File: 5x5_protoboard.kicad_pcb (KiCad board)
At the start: 2 copper layers, 50 x 50 mm, 90 parts, among them CON1 BARREL_JACK, CON2 USB-MINI-B, CON3 USB-MICRO, J1 PINS_3X1, J10 PINS_3X1, J11 PINS_3X1, J12 PINS_3X1, J13 PINS_3X1, J14 PINS_3X1, J15 PINS_3X1, J16 PINS_3X1, J17 PINS_3X1, J18 PINS_3X1, J19 PINS_3X1, J2 PINS_3X1, J20 PINS_3X1, J21 PINS_3X1, J22 PINS_3X1, J23 PINS_3X1, J24 PINS_3X1, J25 PINS_3X1, J26 PINS_3X1, J27 PINS_3X1, J28 PINS_3X1, J29 PINS_3X1, J3 PINS_3X1, J30 PINS_3X1, J31 PINS_3X1, J32 PINS_3X1, J33 PINS_3X1, J34 PINS_3X1, J35 PINS_3X1, J36 PINS_3X1, J37 PINS_3X1, J38 PINS_3X1, J39 PINS_3X1, J4 PINS_3X1, J40 PINS_3X1, J41 PINS_3X1, J42 PINS_3X1, J43 PINS_3X1, J44 PINS_3X1, J45 PINS_3X1, J46 PINS_3X1, J47 PINS_3X1, J48 PINS_3X1, J49 PINS_3X1, J5 PINS_3X1, J50 PINS_3X1, J51 PINS_3X1, J52 PINS_3X1, J53 PINS_3X1, J54 PINS_3X1, J55 PINS_3X1, J56 PINS_3X1, J57 PINS_3X1, J58 PINS_3X1, J59 PINS_3X1, J6 PINS_3X1, J60 PINS_3X1, J61 PINS_3X1, J62 PINS_3X1, J63 PINS_3X1, J64 PINS_3X1, J65 PINS_2X1, J7 PINS_3X1, J8 PINS_3X1, J9 PINS_3X1, P1 CONN_5, U1 7805

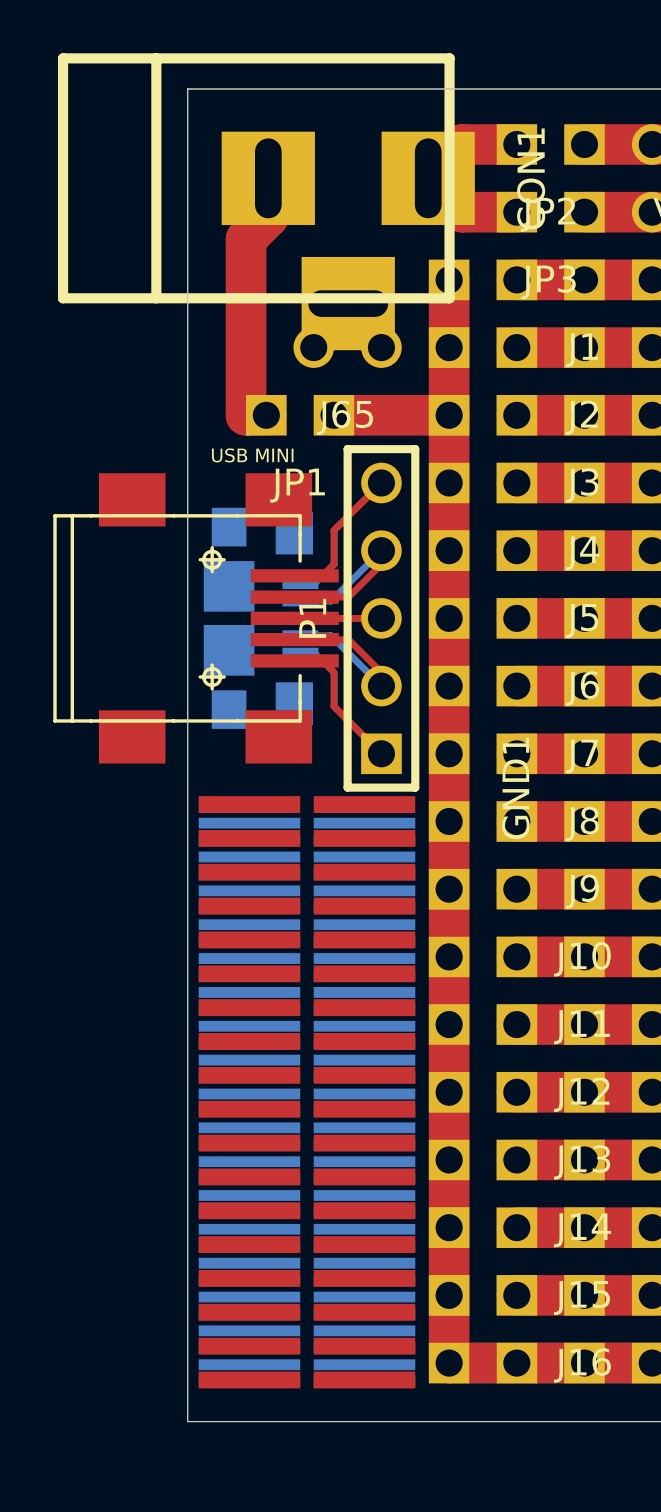
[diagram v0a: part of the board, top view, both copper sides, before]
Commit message: added pads for PTC 1812(SMD) fuse on both sides of the PCB between GND and the barrel jack on the same spot as the jumper and in parallel with it and eachother
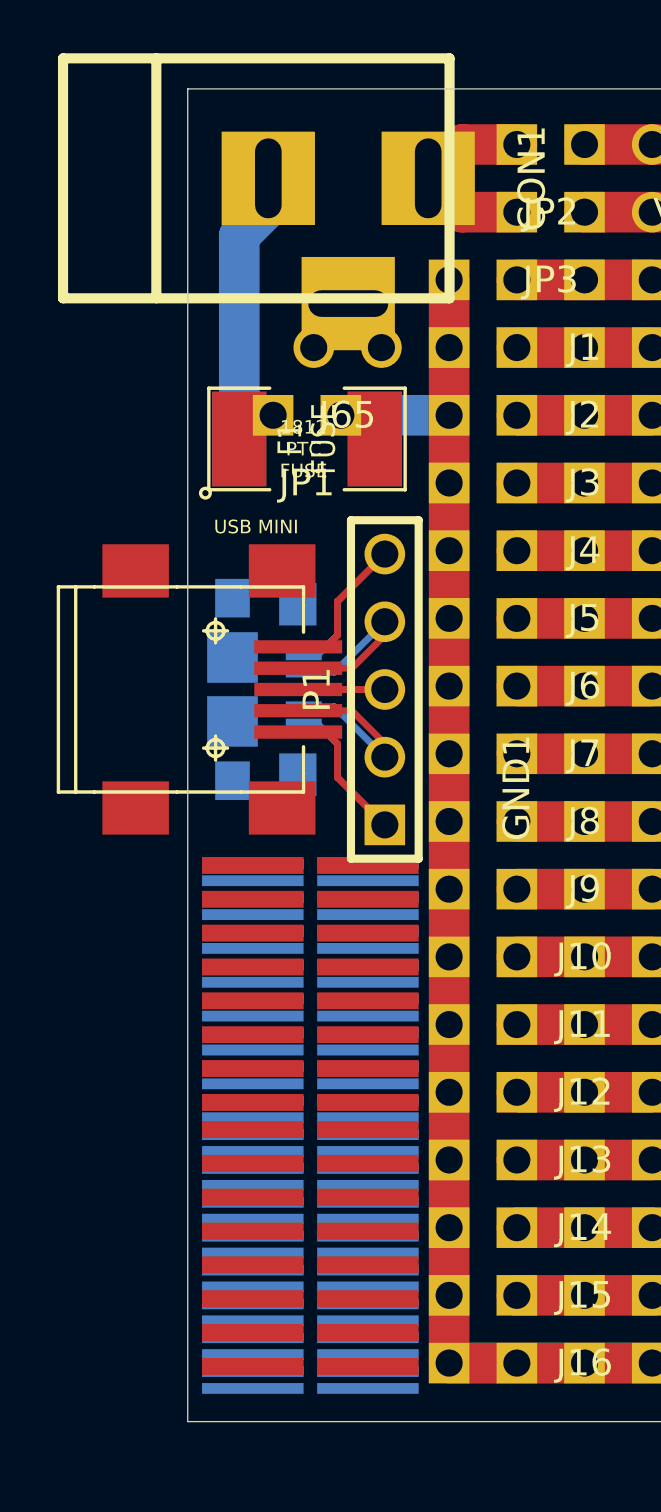
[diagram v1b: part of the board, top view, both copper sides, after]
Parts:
- removed the Ref** at (34.0, 49.5)
- removed the Ref** at (34.0, 49.9)
- added F1: FUSE, SM1812L, F.Cu at (34.0, 35.2)
- added F2: FUSE, SM1812L, B.Cu at (34.0, 35.2)
- moved CON3 2.67 mm to (31.2, 44.6)
- moved P1 2.67 mm to (37.0, 44.6)
- moved CON2 2.67 mm to (30.6, 44.6)
- moved Ref** 0.52 mm to (34.2, 65.5)
- moved Ref** 0.28 mm to (34.2, 55.6)
- moved Ref** 0.28 mm to (34.2, 68.6)
- moved Ref** 0.28 mm to (34.2, 58.4)
- moved Ref** 0.28 mm to (34.2, 53.3)
- moved Ref** 0.28 mm to (34.2, 63.5)
- moved JP1 0.25 mm to (34.0, 34.3)
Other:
- board text added: "1812 PTC"
- board text added: "1812 PTC FUSE"

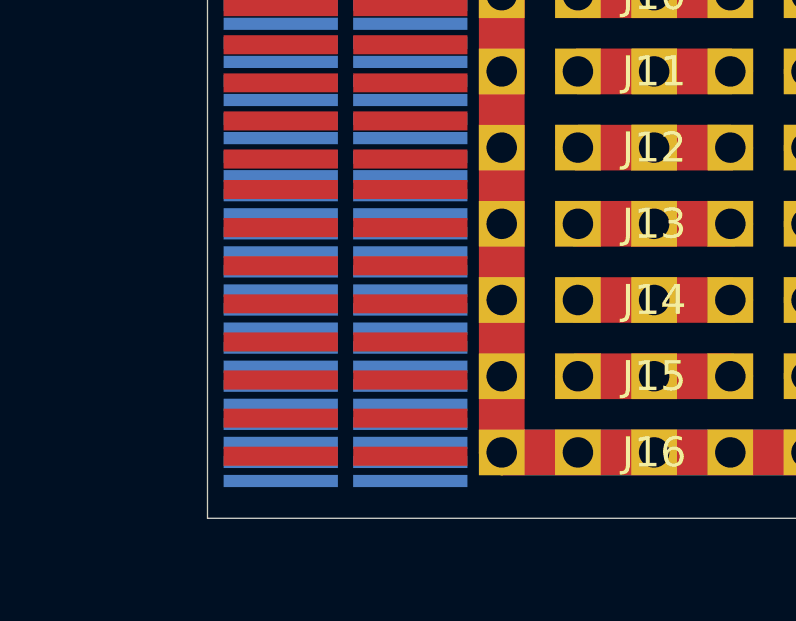
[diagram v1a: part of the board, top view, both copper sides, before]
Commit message: fixed SMD 1.27mm alignment and removed some accidental text on F.Mask
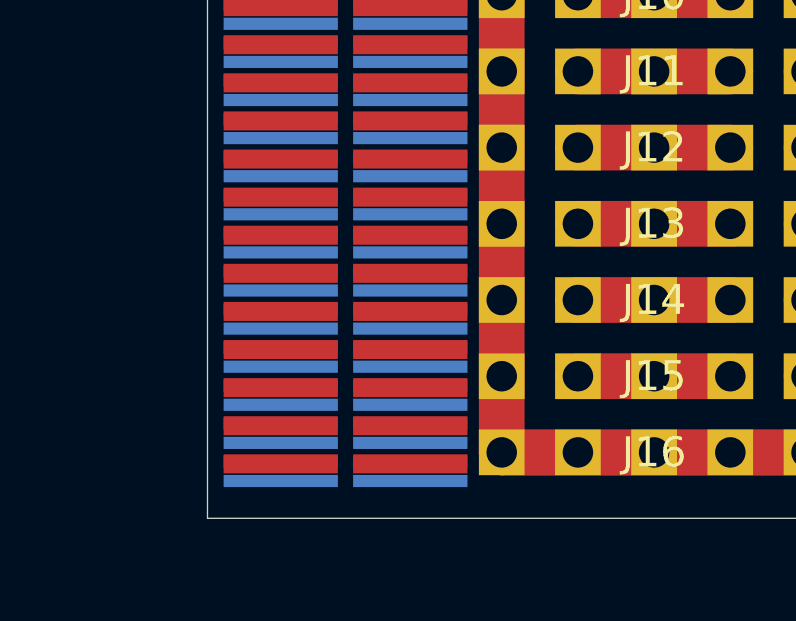
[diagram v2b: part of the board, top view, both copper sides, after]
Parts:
- moved Ref** 0.25 mm to (34.2, 65.8)
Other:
- board text removed: "1812 PTC"
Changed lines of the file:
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@@
     (links 236)
     (no_connects 158)
-    (area 29.549299 22.033299 79.574701 72.058701)
+    (area 24.391619 18.53692 80.839 73.219)
     (thickness 1.6)
-    (drawings 10)
+    (drawings 9)
     (tracks 115)
     (zones 0)
@@
     (pad_to_mask_clearance 0)
     (aux_axis_origin 0 0)
-    (visible_elements FFFFFF8F)
+    (visible_elements FFFFFE8F)
     (pcbplotparams
       (layerselection 284196865)
@@
       (drillshape 0)
       (scaleselection 1)
-      (outputdirectory 5x5_protoboard/))
+      (outputdirectory 5x5_protoboard_v1/))
   )
   (net 0 "")
@@
   )
   (module SMD_127_381_8X2 (layer F.Cu)
-    (at 34.163 65.532)
+    (at 34.163 65.786)
     (fp_text reference Ref** (at 0 0) (layer F.SilkS) hide
       (effects (font (size 1 1) (thickness 0.15)))
@@
     (effects (font (size 0.508 0.508) (thickness 0.127)))
   )
-  (gr_text "1812\nPTC" (at 33.782 36.449) (layer F.Mask)
-    (effects (font (size 0.2 0.2) (thickness 0.05)) (justify mirror))
-  )
   (gr_text "USB MICRO" (at 32.639 39.751) (layer B.SilkS)

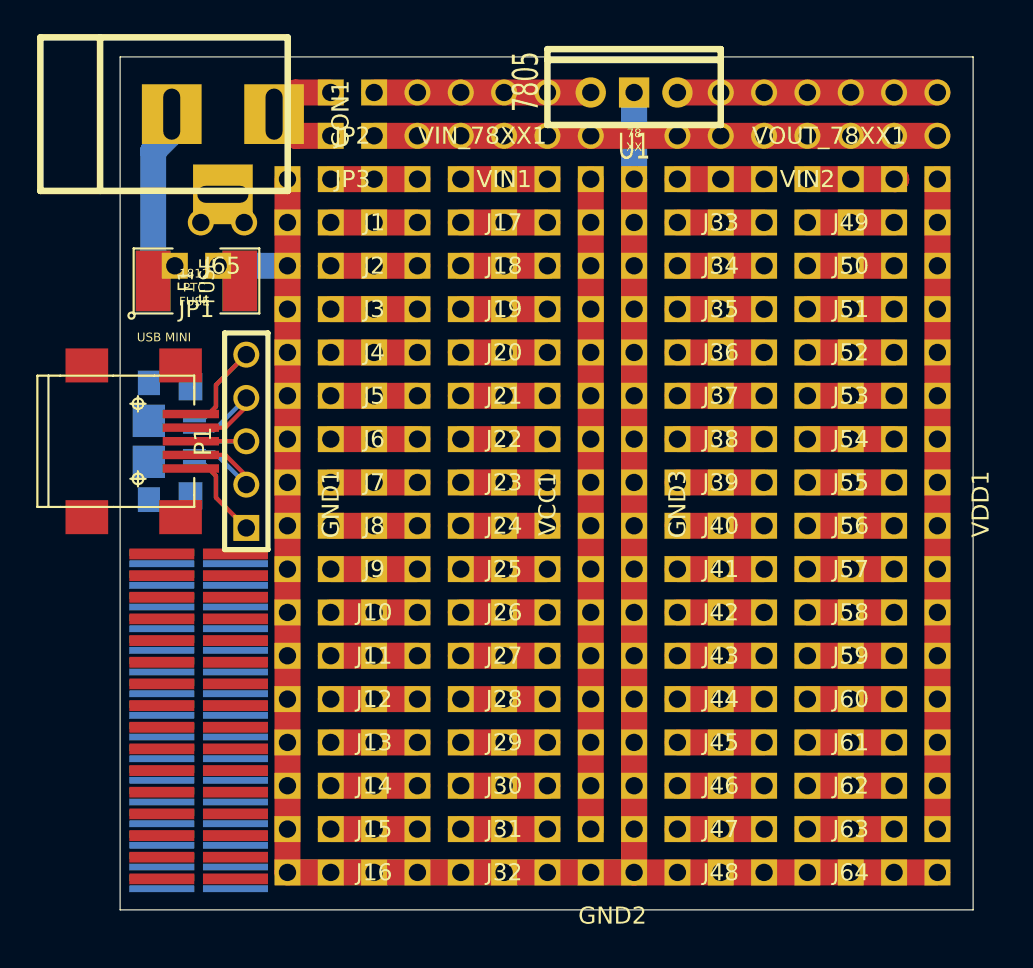
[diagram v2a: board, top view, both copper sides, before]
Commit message: fixed usb pin header alignment to the other pads and the added traces to both sides of the interconnects
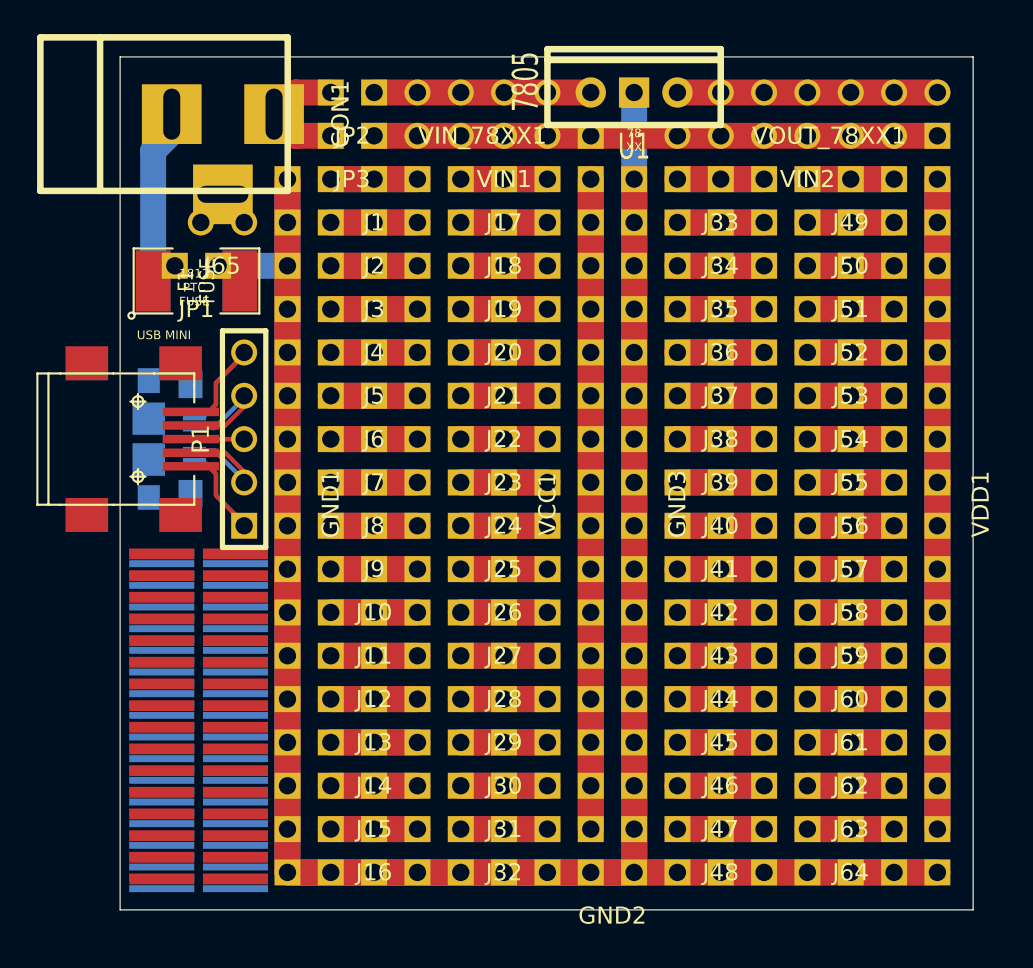
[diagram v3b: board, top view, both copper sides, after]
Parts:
- moved P1 0.18 mm to (36.8, 44.5)
- moved CON2 0.13 mm to (30.6, 44.5)
- moved CON3 0.13 mm to (31.2, 44.5)
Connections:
- U1 pad 1: (no net) -> N-0000056
- U1 pad 2: (no net) -> N-0000084
- U1 pad 3: (no net) -> N-0000059
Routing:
- net N-0000084: track 230.1 -> 352.0 mm
- net N-0000042: track 38.1 -> 76.2 mm
- net N-0000041: track 38.1 -> 76.2 mm
- net N-0000059: track 0.00 -> 15.2 mm
- net (no net): track 21.5 -> 6.29 mm
- net N-0000086: track 5.08 -> 10.2 mm
- net N-0000082: track 5.08 -> 10.2 mm
- net N-0000081: track 5.08 -> 10.2 mm
- net N-0000079: track 5.08 -> 10.2 mm
- net N-0000076: track 5.08 -> 10.2 mm
- net N-0000074: track 5.08 -> 10.2 mm
- net N-0000066: track 5.08 -> 10.2 mm
- net N-0000058: track 5.08 -> 10.2 mm
- net N-0000054: track 5.08 -> 10.2 mm
- net N-0000052: track 5.08 -> 10.2 mm
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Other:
- net class Interconnect removed
- net class Power added: clearance 0.254, trace_width 1.524, via_dia 0.889, via_drill 0.635

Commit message: recreated board using interconnect modules increased rails/triplet pad size, added solder jumper in addition to pin jumpers and added text for USB micro/mini pinout
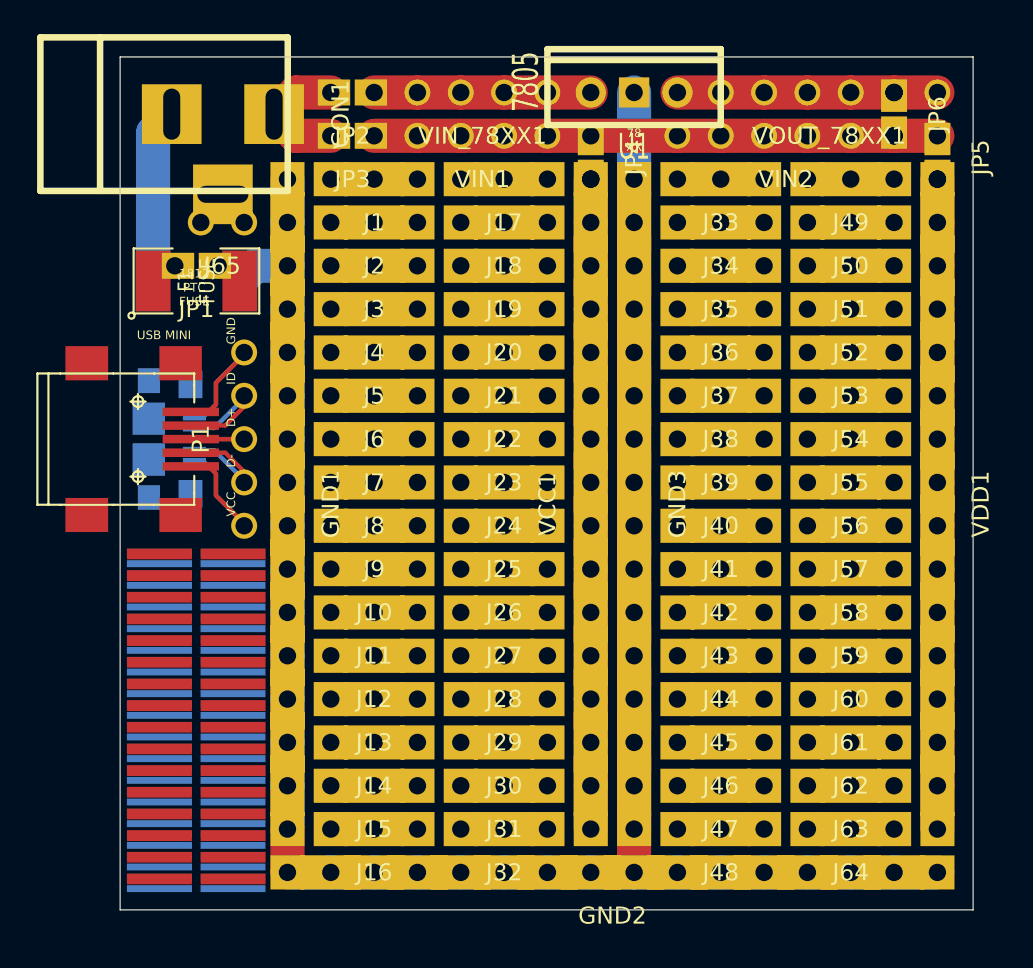
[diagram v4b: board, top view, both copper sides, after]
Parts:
- added JP4: JUMPER, PINS_RECT_2X1_SOLDER_JUMPER, F.Cu at (57.1, 27.9)
- added JP5: JUMPER, PINS_RECT_2X1_SOLDER_JUMPER, F.Cu at (77.5, 27.9)
- added JP6: JUMPER, PINS_RECT_2X1_SOLDER_JUMPER, F.Cu at (74.9, 25.4)
- CON2: footprint dp_devices-CONN_USB_MINI-B -> CONN_USB_MINI-B
- CON3: footprint dp_devices-CONN_USB_MICRO-B -> CONN_USB_MICRO-B
- GND1, GND2, GND3, VCC1, VDD1: footprint PINS_RECT_16X1 -> PINS_INTERCONNECT_16X1
- J1, J10, J11, J12, J13, J14, J15, J16, J17, J18, J19, J2, J20, J21, J22, J23, J24, J25, J26, J27, J28, J29, J3, J30, J31, J32, J33, J34, J35, J36, J37, J38, J39, J4, J40, J41, J42, J43, J44, J45, J46, J47, J48, J49, J5, J50, J51, J52, J53, J54, J55, J56, J57, J58, J59, J6, J60, J61, J62, J63, J64, J7, J8, J9: footprint PINS_RECT_3X1 -> PINS_INTERCONNECT_3X1
- JP1, JP2, JP3: footprint PINS_RECT_2X1 -> PINS_RECT_2X1_SOLDER_JUMPER
- P1: footprint PIN_ARRAY_5x1 -> PINS_5X1
- U1: footprint TO220_VERT -> 7805_VERT
- VIN1: value PINS_5X1 -> PINS_4X1; footprint PINS_5X1 -> PINS_4X1
- VIN2: value PINS_7X1 -> PINS_6X1; footprint PINS_7X1 -> PINS_6X1
- moved VIN1 1.27 mm to (50.8, 26.7)
- moved VIN2 1.27 mm to (68.6, 26.7)
- moved Ref** 0.14 mm to (34.0, 65.8)
- moved Ref** 0.14 mm to (34.0, 55.6)
- moved Ref** 0.14 mm to (34.0, 68.6)
- moved Ref** 0.14 mm to (34.0, 63.5)
- moved Ref** 0.14 mm to (34.0, 58.4)
- moved Ref** 0.14 mm to (34.0, 53.3)
- turned P1 to 270 degrees
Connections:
- F1 pad 2: N-0000084 (its old number) -> N-0000083
- F2 pad 2: N-0000084 (its old number) -> N-0000083
- GND1 pad 1: N-0000084 (its old number) -> N-0000083
- GND1 pad 10: N-0000084 (its old number) -> N-0000083
- GND1 pad 11: N-0000084 (its old number) -> N-0000083
- GND1 pad 12: N-0000084 (its old number) -> N-0000083
- GND1 pad 13: N-0000084 (its old number) -> N-0000083
- GND1 pad 14: N-0000084 (its old number) -> N-0000083
- GND1 pad 15: N-0000084 (its old number) -> N-0000083
- GND1 pad 16: N-0000084 (its old number) -> N-0000083
- GND1 pad 2: N-0000084 (its old number) -> N-0000083
- GND1 pad 3: N-0000084 (its old number) -> N-0000083
- GND1 pad 4: N-0000084 (its old number) -> N-0000083
- GND1 pad 5: N-0000084 (its old number) -> N-0000083
- GND1 pad 6: N-0000084 (its old number) -> N-0000083
- GND1 pad 7: N-0000084 (its old number) -> N-0000083
- GND1 pad 8: N-0000084 (its old number) -> N-0000083
- GND1 pad 9: N-0000084 (its old number) -> N-0000083
- GND2 pad 1: N-0000084 (its old number) -> N-0000083
- GND2 pad 10: N-0000084 (its old number) -> N-0000083
- GND2 pad 11: N-0000084 (its old number) -> N-0000083
- GND2 pad 12: N-0000084 (its old number) -> N-0000083
- GND2 pad 13: N-0000084 (its old number) -> N-0000083
- GND2 pad 14: N-0000084 (its old number) -> N-0000083
- GND2 pad 15: N-0000084 (its old number) -> N-0000083
- GND2 pad 16: N-0000084 (its old number) -> N-0000083
- GND2 pad 2: N-0000084 (its old number) -> N-0000083
- GND2 pad 3: N-0000084 (its old number) -> N-0000083
- GND2 pad 4: N-0000084 (its old number) -> N-0000083
- GND2 pad 5: N-0000084 (its old number) -> N-0000083
- GND2 pad 6: N-0000084 (its old number) -> N-0000083
- GND2 pad 7: N-0000084 (its old number) -> N-0000083
- GND2 pad 8: N-0000084 (its old number) -> N-0000083
- GND2 pad 9: N-0000084 (its old number) -> N-0000083
- GND3 pad 1: N-0000084 (its old number) -> N-0000083
- GND3 pad 10: N-0000084 (its old number) -> N-0000083
- GND3 pad 11: N-0000084 (its old number) -> N-0000083
- GND3 pad 12: N-0000084 (its old number) -> N-0000083
- GND3 pad 13: N-0000084 (its old number) -> N-0000083
- GND3 pad 14: N-0000084 (its old number) -> N-0000083
- GND3 pad 15: N-0000084 (its old number) -> N-0000083
- GND3 pad 16: N-0000084 (its old number) -> N-0000083
- GND3 pad 2: N-0000084 (its old number) -> N-0000083
- GND3 pad 3: N-0000084 (its old number) -> N-0000083
- GND3 pad 4: N-0000084 (its old number) -> N-0000083
- GND3 pad 5: N-0000084 (its old number) -> N-0000083
- GND3 pad 6: N-0000084 (its old number) -> N-0000083
- GND3 pad 7: N-0000084 (its old number) -> N-0000083
- GND3 pad 8: N-0000084 (its old number) -> N-0000083
- GND3 pad 9: N-0000084 (its old number) -> N-0000083
- JP1 pad 2: N-0000084 (its old number) -> N-0000083
- JP2 pad 2: N-0000056 (its old number) -> N-0000060
- JP3 pad 2: N-0000060 -> N-0000059
- P1 pad 1: N-000003 -> N-000006
- P1 pad 2: N-000002 -> N-0000011
- P1 pad 3: N-000001 -> N-0000012
- P1 pad 4: N-0000010 -> N-0000057
- P1 pad 5: N-0000011 -> N-000005
- VIN1 pad 1: N-0000060 -> N-0000059
- VIN1 pad 2: N-0000060 -> N-0000059
- VIN1 pad 3: N-0000060 -> N-0000059
- VIN1 pad 4: N-0000060 -> N-0000059
- VIN2 pad 1: N-0000060 -> N-0000059
- VIN2 pad 2: N-0000060 -> N-0000059
- VIN2 pad 3: N-0000060 -> N-0000059
- VIN2 pad 4: N-0000060 -> N-0000059
- VIN2 pad 5: N-0000060 -> N-0000059
- VIN2 pad 6: N-0000060 -> N-0000059
- VIN_78XX1 pad 1: N-0000056 (its old number) -> N-0000060
- VIN_78XX1 pad 2: N-0000056 (its old number) -> N-0000060
- VIN_78XX1 pad 3: N-0000056 (its old number) -> N-0000060
- VIN_78XX1 pad 4: N-0000056 (its old number) -> N-0000060
- VOUT_78XX1 pad 1: N-0000059 -> N-0000058
- VOUT_78XX1 pad 2: N-0000059 -> N-0000058
- VOUT_78XX1 pad 3: N-0000059 -> N-0000058
- VOUT_78XX1 pad 4: N-0000059 -> N-0000058
- VOUT_78XX1 pad 5: N-0000059 -> N-0000058
- VOUT_78XX1 pad 6: N-0000059 -> N-0000058
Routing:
- net N-0000084 (its old number): track 352.0 -> 0.00 mm
- net N-0000083: track 0.00 -> 127.6 mm
- net N-0000041: track 76.2 -> 38.1 mm
- net N-0000039: track 76.2 -> 38.1 mm
- net N-0000060: track 33.0 -> 12.7 mm
- net N-0000059: track 15.2 -> 33.0 mm
- net N-0000058: track 0.00 -> 15.2 mm
- net N-0000056 (its old number): track 12.7 -> 0.00 mm
- net N-000005: track 0.00 -> 10.8 mm
- net N-000003: track 10.8 -> 0.00 mm
- net N-000006: track 0.00 -> 10.8 mm
- net N-0000085: track 10.2 -> 0.00 mm
- net N-0000082: track 10.2 -> 0.00 mm
- net N-0000080: track 10.2 -> 0.00 mm
- net N-0000078: track 10.2 -> 0.00 mm
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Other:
- net class Power: trace_width 1.524 -> 2
- board text added: "D+"
- board text added: "D-"
- board text added: "GND"
- board text added: "ID"
- board text added: "VCC"
